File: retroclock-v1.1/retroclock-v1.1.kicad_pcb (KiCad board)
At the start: 4 copper layers, 147.5 x 108 mm, 22 parts, among them J1 Hours, J2 Mins, J3 Secs, J4 Nixie YY2, J5 Nixie YY1, J6 Nixie MM2, J7 Nixie MM1, J8 Nixie DD2, J9 Nixie DD1

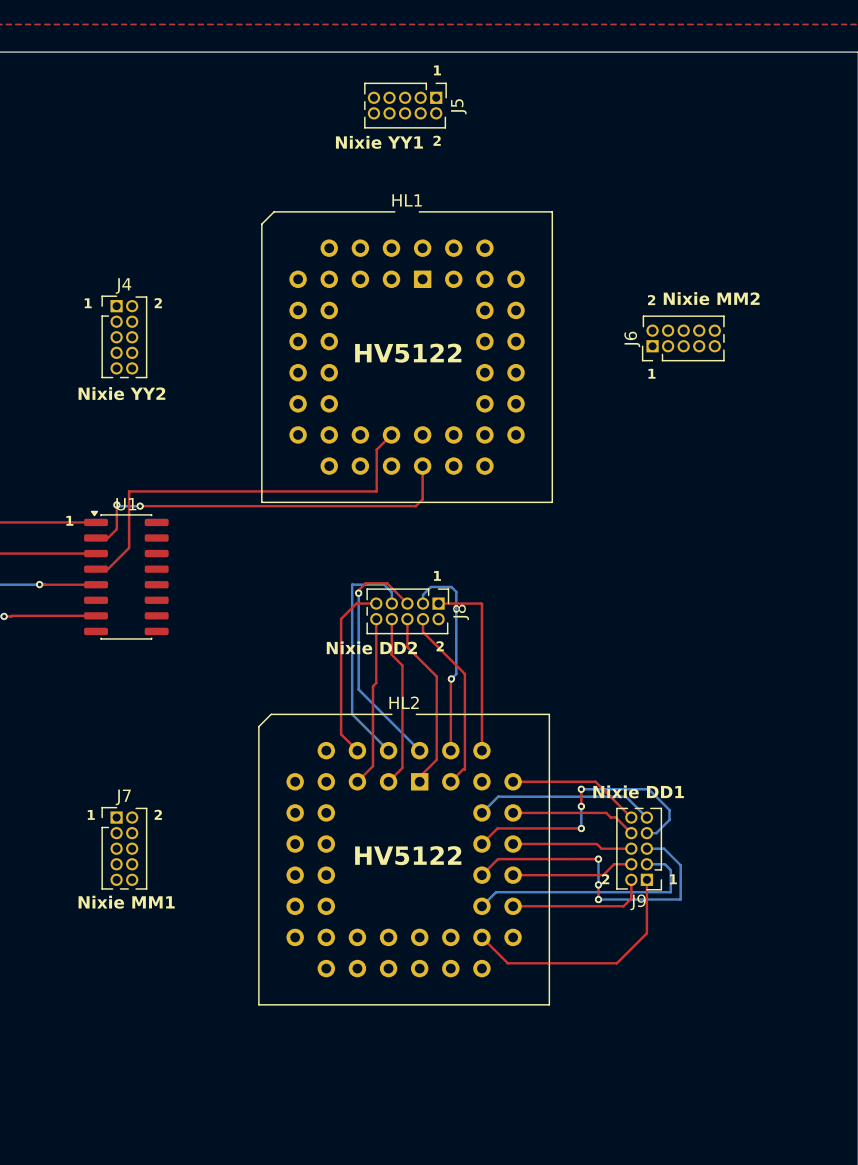
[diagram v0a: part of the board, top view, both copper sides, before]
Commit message: finished routing, no errors
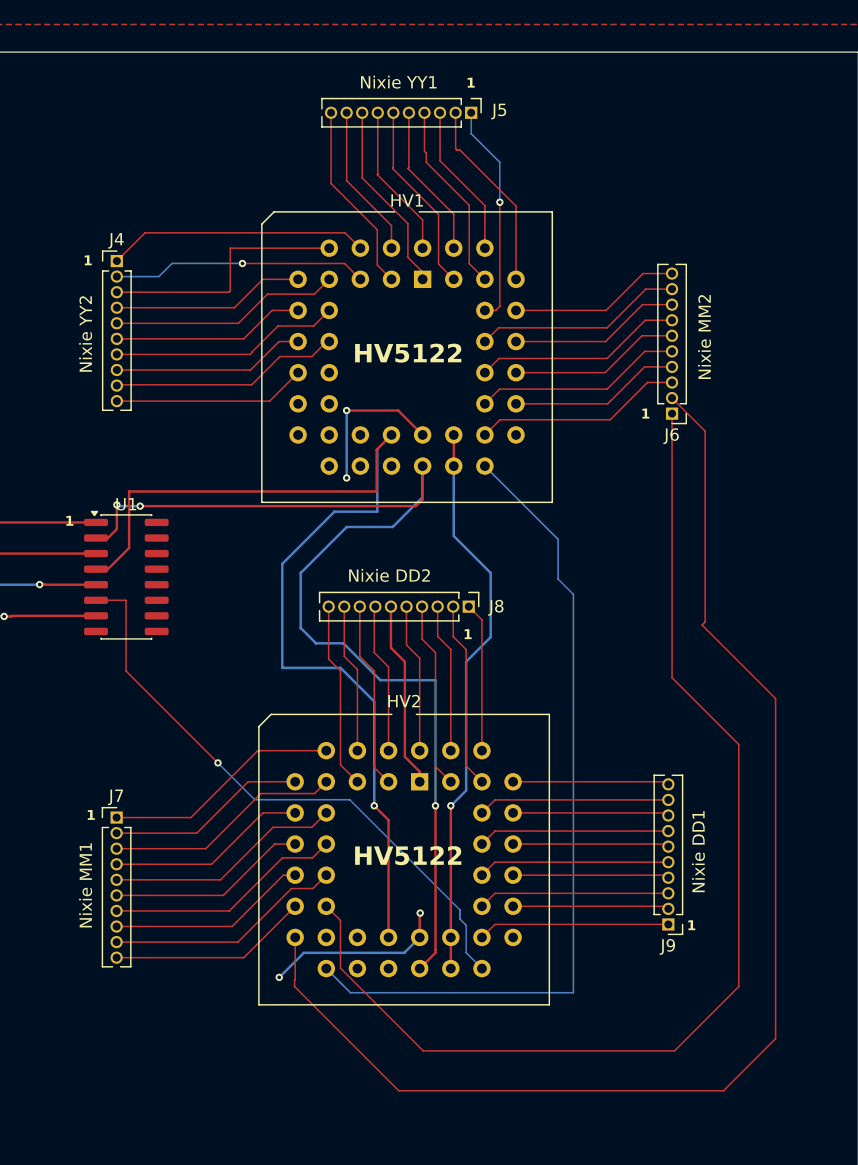
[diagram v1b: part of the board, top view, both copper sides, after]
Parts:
- J4, J5, J6, J7, J8, J9: footprint Connector_PinHeader_1.27mm:PinHeader_2x05_P1.27mm_Vertical -> Connector_PinHeader_1.27mm:PinHeader_1x10_P1.27mm_Vertical
- moved J6 5.73 mm to (208.8, 67.8), turned to 180 degrees
- moved J9 4.04 mm to (208.5, 109.4)
- moved J4 3.68 mm to (163.5, 55.3)
- moved J5 3.10 mm to (192.4, 43.2)
- moved J8 2.48 mm to (192.2, 83.5)
- renumbered HL1 to HV1, HL2 to HV2
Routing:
- net Net-(J6-Pin_2): track 0.00 -> 104.5 mm
- net Net-(HL2-HVO31): track 0.00 -> 92.0 mm
- net Net-(HL1-D_IN): track 0.00 -> 66.9 mm
- net Net-(HL1-CLK): track 31.9 -> 88.3 mm, vias 2 -> 3
- net Net-(HL1-OE): track 33.3 -> 86.5 mm, vias 0 -> 1
- net Net-(HL2-D_IN): track 0.00 -> 49.1 mm, vias 0 -> 1
- net +12V: track 0.00 -> 46.1 mm, vias 0 -> 1
- net GND: track 0.00 -> 27.4 mm, vias 0 -> 4
- net Net-(HL1-HVO19): track 0.00 -> 21.3 mm
- net Net-(HL1-HVO21): track 0.00 -> 20.9 mm
- net Net-(HL1-HVO20): track 0.00 -> 20.8 mm, vias 0 -> 1
- net Net-(HL2-HVO29): track 0.00 -> 19.4 mm
- net Net-(HL2-HVO25): track 0.00 -> 19.4 mm
- net Net-(J7-Pin_3): track 0.00 -> 19.4 mm
- net Net-(HL2-HVO27): track 0.00 -> 19.4 mm
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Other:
- board text added: "J8"
- board text removed: "2"

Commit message: retroclock 1.1 sent to JLCPCB!
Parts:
- added C10: 100nF, Capacitor_THT:C_Disc_D3.4mm_W2.1mm_P2.50mm, F.Cu at (144.3, 84.0)
- added C11: 100nF, Capacitor_THT:C_Disc_D3.4mm_W2.1mm_P2.50mm, F.Cu at (161.8, 107.3)
- added C12: 68uF, Capacitor_THT:CP_Radial_D8.0mm_P3.80mm, F.Cu at (161.4, 97.5)
- added C13: 100uF, Capacitor_THT:CP_Radial_D10.0mm_P5.00mm, F.Cu at (126.5, 97.3)
- added C14: 100nF, Capacitor_THT:C_Rect_L18.0mm_W7.0mm_P15.00mm_FKS3_FKP3, F.Cu at (118.8, 98.8)
- added C15: 10uF, Capacitor_THT:CP_Radial_D8.0mm_P3.80mm, F.Cu at (132.0, 78.0)
- added C16: 10uF, Capacitor_THT:CP_Radial_D8.0mm_P3.80mm, F.Cu at (146.0, 72.4)
- added C4: 100n, Capacitor_THT:C_Disc_D3.4mm_W2.1mm_P2.50mm, F.Cu at (173.3, 89.2)
- added C5: 100n, Capacitor_SMD:C_1206_3216Metric_Pad1.33x1.80mm_HandSolder, B.Cu at (205.2, 90.0)
- added C6: 100n, Capacitor_THT:C_Disc_D3.4mm_W2.1mm_P2.50mm, F.Cu at (178.6, 91.8)
- added C7: 100n, Capacitor_SMD:C_1206_3216Metric_Pad1.33x1.80mm_HandSolder, B.Cu at (208.7, 68.5)
- added C8: 100n, Capacitor_THT:C_Disc_D3.4mm_W2.1mm_P2.50mm, F.Cu at (183.4, 111.4)
- added C9: 100n, Capacitor_THT:C_Disc_D3.4mm_W2.1mm_P2.50mm, F.Cu at (177.6, 111.4)
- added D1: LED, LED_THT:LED_D3.0mm_Clear, F.Cu at (191.2, 46.5)
- added D2: LED, LED_THT:LED_D3.0mm_Clear, F.Cu at (128.9, 67.8)
- added D3: RF01VM2S, Diode_THT:D_DO-15_P15.24mm_Horizontal, F.Cu at (125.8, 110.3)
- added D4: LED, LED_THT:LED_D3.0mm_Clear, F.Cu at (172.2, 111.4)
- added D5: LED, LED_THT:LED_D3.0mm_Clear, F.Cu at (187.1, 111.4)
- added DCFRx1: ~, 01_mjc_library:DCF77Rx_A, F.Cu at (121.6, 50.0)
- added G***: LOGO, 01_mjc_library:doomsday_clock, F.Cu at (139.5, 48.3)
- added H1: MountingHole, MountingHole:MountingHole_2.2mm_M2_Pad, F.Cu at (81.0, 45.0)
- added H2: MountingHole, MountingHole:MountingHole_2.2mm_M2_Pad, F.Cu at (81.0, 114.0)
- added H3: MountingHole, MountingHole:MountingHole_2.2mm_M2_Pad, F.Cu at (227.0, 45.0)
- added H4: MountingHole, MountingHole:MountingHole_2.2mm_M2_Pad, F.Cu at (227.0, 114.0)
- added J10: Serial DBG, Connector_PinHeader_2.54mm:PinHeader_1x03_P2.54mm_Vertical, F.Cu at (181.0, 50.6)
- added J11: DCF DBG, Connector_Molex:Molex_KK-254_AE-6410-02A_1x02_P2.54mm_Vertical, F.Cu at (119.2, 65.8)
- added J12: Supply, Connector_Molex:Molex_KK-254_AE-6410-03A_1x03_P2.54mm_Vertical, F.Cu at (174.5, 104.2)
- added J13: 170V, Connector_Molex:Molex_KK-254_AE-6410-02A_1x02_P2.54mm_Vertical, F.Cu at (117.3, 105.0)
- added J14: ~, 01_mjc_library:Jumper 2.54 2x03, F.Cu at (160.0, 86.4)
- added J15: 3v3 src, Connector_PinHeader_2.54mm:PinHeader_1x03_P2.54mm_Vertical, F.Cu at (151.9, 77.0)
- added L1: 100H, Inductor_THT:L_Radial_D10.0mm_P5.00mm_Neosid_SD12k_style3, F.Cu at (153.8, 107.5)
- added LVL1: ~, Package_SO:SOIC-16_3.9x9.9mm_P1.27mm, F.Cu at (175.9, 81.7)
- added MAX1: MAX1771, Package_SO:SOIC-8_3.9x4.9mm_P1.27mm, F.Cu at (148.3, 89.0)
- added Q1: ~, 01_mjc_library:MOSFET, F.Cu at (148.1, 97.3)
- added R10: 1.2M, Resistor_THT:R_Axial_DIN0204_L3.6mm_D1.6mm_P7.62mm_Horizontal, F.Cu at (126.0, 105.0)
- added R11: 10k, Resistor_THT:R_Axial_DIN0204_L3.6mm_D1.6mm_P7.62mm_Horizontal, F.Cu at (137.8, 105.0)
- added R12: 0.2, Resistor_THT:R_Axial_DIN0204_L3.6mm_D1.6mm_P7.62mm_Horizontal, F.Cu at (137.4, 84.5)
- added R13: R, Resistor_THT:R_Axial_DIN0204_L3.6mm_D1.6mm_P7.62mm_Horizontal, F.Cu at (98.7, 46.9)
- added R14: R, Resistor_THT:R_Axial_DIN0204_L3.6mm_D1.6mm_P7.62mm_Horizontal, F.Cu at (98.7, 52.9)
- added R15: R, Resistor_THT:R_Axial_DIN0204_L3.6mm_D1.6mm_P7.62mm_Horizontal, F.Cu at (98.7, 68.3)
- added R16: R, Resistor_THT:R_Axial_DIN0204_L3.6mm_D1.6mm_P7.62mm_Horizontal, F.Cu at (98.8, 74.3)
- added R17: R, Resistor_THT:R_Axial_DIN0204_L3.6mm_D1.6mm_P7.62mm_Horizontal, F.Cu at (94.9, 97.5)
- added R18: R, Resistor_THT:R_Axial_DIN0204_L3.6mm_D1.6mm_P7.62mm_Horizontal, F.Cu at (101.4, 97.5)
- added R19: R, Resistor_THT:R_Axial_DIN0204_L3.6mm_D1.6mm_P7.62mm_Horizontal, F.Cu at (170.1, 115.9)
- added R20: R, Resistor_THT:R_Axial_DIN0204_L3.6mm_D1.6mm_P7.62mm_Horizontal, F.Cu at (188.4, 115.9)
- added R7: R, Resistor_THT:R_Axial_DIN0204_L3.6mm_D1.6mm_P7.62mm_Horizontal, F.Cu at (185.6, 52.0)
- added R8: R, Resistor_THT:R_Axial_DIN0204_L3.6mm_D1.6mm_P7.62mm_Horizontal, F.Cu at (123.9, 69.4)
- added R9: 0.2, Resistor_THT:R_Axial_DIN0204_L3.6mm_D1.6mm_P7.62mm_Horizontal, F.Cu at (137.3, 88.8)
- C1, C2, C3: footprint Capacitor_THT:CP_Axial_L18.0mm_D6.5mm_P25.00mm_Horizontal -> Capacitor_THT:C_Axial_L19.0mm_D7.5mm_P25.00mm_Horizontal
- ESP1: footprint mjc_library:ESP32 Header -> 01_mjc_library:ESP32 Header
- HV1, HV2: footprint mjc_library:PLCC-44_THT-Socket -> 01_mjc_library:PLCC44 MillMaxMfg 940
- J1, J2, J3: footprint Connector_PinHeader_1.27mm:PinHeader_1x02_P1.27mm_Vertical -> Connector_Molex:Molex_KK-254_AE-6410-02A_1x02_P2.54mm_Vertical
- J4, J6, J7, J8: footprint Connector_PinHeader_1.27mm:PinHeader_1x10_P1.27mm_Vertical -> Connector_PinHeader_2.54mm:PinHeader_2x07_P2.54mm_Vertical
- J5: value Nixie YY1 -> Nixie DD1; footprint Connector_PinHeader_1.27mm:PinHeader_1x10_P1.27mm_Vertical -> Connector_PinHeader_2.54mm:PinHeader_2x07_P2.54mm_Vertical
- J9: value Nixie DD1 -> Nixie YY1; footprint Connector_PinHeader_1.27mm:PinHeader_1x10_P1.27mm_Vertical -> Connector_PinHeader_2.54mm:PinHeader_2x07_P2.54mm_Vertical
- R1, R2, R3, R4, R5, R6: footprint Resistor_THT:R_Axial_DIN0207_L6.3mm_D2.5mm_P7.62mm_Horizontal -> Resistor_THT:R_Axial_DIN0204_L3.6mm_D1.6mm_P7.62mm_Horizontal
- U1: footprint Package_SO:SOIC-16_3.9x9.9mm_P1.27mm -> 01_mjc_library:HT7333
- moved J4 79.2 mm to (228.3, 100.9), turned to 180 degrees
- moved J7 46.5 mm to (184.9, 59.4)
- moved HV1 46.0 mm to (205.8, 99.4), turned to 180 degrees
- moved J5 46.0 mm to (228.3, 71.9), turned to 180 degrees
- moved J8 44.4 mm to (214.3, 45.0)
- moved HV2 43.4 mm to (208.3, 59.3)
- moved J6 31.7 mm to (185.0, 88.7), turned to 0 degrees
- moved ESP1 27.3 mm to (162.9, 59.8)
- moved U1 25.2 mm to (139.3, 78.3)
- moved C1 18.0 mm to (106.2, 61.9), turned to 180 degrees
- moved C2 17.2 mm to (106.4, 83.3), turned to 180 degrees
- moved C3 16.7 mm to (106.2, 106.4), turned to 180 degrees
- moved R3 12.5 mm to (98.7, 71.3)
- moved J3 11.9 mm to (83.4, 97.9), turned to 90 degrees
- moved J2 11.9 mm to (84.5, 74.0), turned to 90 degrees
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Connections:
- net Net-(ESP1-G10) renamed AM_HRS
- net Net-(ESP1-G20) renamed AM_MIN
- net Net-(ESP1-G21) renamed AM_SEC
- net Net-(J1-Pin_2) renamed /ammeter_driver/AM_H-
- net Net-(J2-Pin_2) renamed /ammeter_driver/AM_M-
- net Net-(J3-Pin_2) renamed /ammeter_driver/AM_S-
- ESP1 pad 1: Net-(ESP1-G5) -> /OE
- ESP1 pad 10: unconnected-(ESP1-G1/A1_1-Pad10) -> /BOOST_EN
- ESP1 pad 3: unconnected-(ESP1-G7-Pad3) -> DCF_PON
- ESP1 pad 4: Net-(ESP1-SDA) -> /SDA
- ESP1 pad 5: Net-(ESP1-SCL) -> /SCL
- ESP1 pad 9: unconnected-(ESP1-G0/A1_0-Pad9) -> DCF_DAT
- HV1 pad 1: Net-(HL1-HVO16) -> Net-(HV1-HVO16)
- HV1 pad 10: Net-(HL1-HVO25) -> Net-(HV1-HVO25)
- HV1 pad 11: Net-(HL1-HVO26) -> Net-(HV1-HVO26)
- HV1 pad 12: Net-(HL1-HVO27) -> Net-(HV1-HVO27)
- HV1 pad 13: Net-(HL1-HVO28) -> Net-(HV1-HVO28)
- HV1 pad 14: unconnected-(HL1-HVO29-Pad14) -> Net-(HV1-HVO29)
- HV1 pad 15: unconnected-(HL1-HVO30-Pad15) -> Net-(HV1-HVO30)
- HV1 pad 16: unconnected-(HL1-HVO31-Pad16) -> Net-(HV1-HVO31)
- HV1 pad 2: Net-(HL1-HVO17) -> Net-(HV1-HVO17)
- HV1 pad 23: Net-(HL1-OE) -> NIX_OE
- HV1 pad 24: Net-(HL1-CLK) -> NIX_CLK
- HV1 pad 3: Net-(HL1-HVO18) -> Net-(HV1-HVO18)
- HV1 pad 30: Net-(HL1-HVO1) -> Net-(HV1-HVO1)
- HV1 pad 31: Net-(HL1-HVO2) -> Net-(HV1-HVO2)
- HV1 pad 32: Net-(HL1-HVO3) -> Net-(HV1-HVO3)
- HV1 pad 33: Net-(HL1-HVO4) -> Net-(HV1-HVO4)
- HV1 pad 34: Net-(HL1-HVO5) -> Net-(HV1-HVO5)
- HV1 pad 35: Net-(HL1-HVO6) -> Net-(HV1-HVO6)
- HV1 pad 36: Net-(HL1-HVO7) -> Net-(HV1-HVO7)
- HV1 pad 37: Net-(HL1-HVO8) -> Net-(HV1-HVO8)
- HV1 pad 38: Net-(HL1-HVO9) -> Net-(HV1-HVO9)
- HV1 pad 39: Net-(HL1-HVO10) -> Net-(HV1-HVO10)
- HV1 pad 4: Net-(HL1-HVO19) -> Net-(HV1-HVO19)
- HV1 pad 40: Net-(HL1-HVO11) -> Net-(HV1-HVO11)
- HV1 pad 41: Net-(HL1-HVO12) -> Net-(HV1-HVO12)
- HV1 pad 42: Net-(HL1-HVO13) -> Net-(HV1-HVO13)
- HV1 pad 43: Net-(HL1-HVO14) -> Net-(HV1-HVO14)
- HV1 pad 44: Net-(HL1-HVO15) -> Net-(HV1-HVO15)
- HV1 pad 5: Net-(HL1-HVO20) -> Net-(HV1-HVO20)
- HV1 pad 6: Net-(HL1-HVO21) -> unconnected-(HV1-HVO21-Pad6)
- HV1 pad 7: Net-(HL1-HVO22) -> Net-(HV1-HVO22)
- HV1 pad 8: Net-(J4-Pin_5) -> Net-(HV1-HVO23)
- HV1 pad 9: Net-(HL1-HVO24) -> Net-(HV1-HVO24)
- HV2 pad 10: Net-(HL2-HVO25) -> Net-(HV2-HVO25)
- HV2 pad 11: Net-(HL2-HVO26) -> Net-(HV2-HVO26)
- HV2 pad 12: Net-(HL2-HVO27) -> Net-(HV2-HVO27)
- HV2 pad 13: Net-(HL2-HVO28) -> Net-(HV2-HVO28)
- HV2 pad 14: Net-(HL2-HVO29) -> Net-(HV2-HVO29)
- HV2 pad 15: Net-(HL2-HVO30) -> Net-(HV2-HVO30)
- HV2 pad 16: Net-(HL2-HVO31) -> Net-(HV2-HVO31)
- HV2 pad 17: Net-(J6-Pin_2) -> unconnected-(HV2-HVO32-Pad17)
- HV2 pad 23: Net-(HL1-OE) -> NIX_OE
- HV2 pad 24: Net-(HL1-CLK) -> NIX_CLK
- HV2 pad 28: Net-(HL2-D_IN) -> NIX_DAT_IN
- HV2 pad 30: Net-(HL2-HVO1) -> Net-(HV2-HVO1)
- HV2 pad 31: Net-(HL2-HVO2) -> Net-(HV2-HVO2)
- HV2 pad 32: Net-(HL2-HVO3) -> Net-(HV2-HVO3)
- HV2 pad 33: Net-(HL2-HVO4) -> Net-(HV2-HVO4)
- HV2 pad 34: Net-(HL2-HVO5) -> Net-(HV2-HVO5)
- HV2 pad 35: Net-(HL2-HVO6) -> Net-(HV2-HVO6)
- HV2 pad 36: Net-(HL2-HVO7) -> Net-(HV2-HVO7)
- HV2 pad 37: Net-(HL2-HVO8) -> Net-(HV2-HVO8)
- HV2 pad 38: Net-(HL2-HVO9) -> Net-(HV2-HVO9)
- HV2 pad 39: Net-(HL2-HVO10) -> Net-(HV2-HVO10)
- HV2 pad 6: Net-(HL2-HVO21) -> unconnected-(HV2-HVO21-Pad6)
- HV2 pad 7: Net-(HL2-HVO22) -> Net-(HV2-HVO22)
- HV2 pad 8: Net-(J7-Pin_3) -> Net-(HV2-HVO23)
- HV2 pad 9: Net-(HL2-HVO24) -> Net-(HV2-HVO24)
- J4 pad 1: Net-(HL1-HVO19) -> Net-(HV1-HVO22)
- J4 pad 10: Net-(HL1-HVO28) -> Net-(HV1-HVO31)
- J4 pad 2: Net-(HL1-HVO20) -> Net-(HV1-HVO23)
- J4 pad 3: Net-(HL1-HVO21) -> Net-(HV1-HVO24)
- J4 pad 4: Net-(HL1-HVO22) -> Net-(HV1-HVO25)
- J4 pad 5: Net-(J4-Pin_5) -> Net-(HV1-HVO26)
- J4 pad 6: Net-(HL1-HVO24) -> Net-(HV1-HVO27)
- J4 pad 7: Net-(HL1-HVO25) -> Net-(HV1-HVO28)
- J4 pad 8: Net-(HL1-HVO26) -> Net-(HV1-HVO29)
- J4 pad 9: Net-(HL1-HVO27) -> Net-(HV1-HVO30)
- J5 pad 1: Net-(HL1-HVO9) -> Net-(HV2-HVO1)
- J5 pad 10: Net-(HL1-HVO18) -> Net-(HV2-HVO10)
- J5 pad 2: Net-(HL1-HVO10) -> Net-(HV2-HVO2)
- J5 pad 3: Net-(HL1-HVO11) -> Net-(HV2-HVO3)
- J5 pad 4: Net-(HL1-HVO12) -> Net-(HV2-HVO4)
- J5 pad 5: Net-(HL1-HVO13) -> Net-(HV2-HVO5)
- J5 pad 6: Net-(HL1-HVO14) -> Net-(HV2-HVO6)
- J5 pad 7: Net-(HL1-HVO15) -> Net-(HV2-HVO7)
- J5 pad 8: Net-(HL1-HVO16) -> Net-(HV2-HVO8)
- J5 pad 9: Net-(HL1-HVO17) -> Net-(HV2-HVO9)
- J6 pad 1: Net-(HL2-HVO31) -> Net-(HV1-HVO1)
- J6 pad 10: Net-(HL1-HVO8) -> Net-(HV1-HVO10)
- J6 pad 2: Net-(J6-Pin_2) -> Net-(HV1-HVO2)
- J6 pad 3: Net-(HL1-HVO1) -> Net-(HV1-HVO3)
- J6 pad 4: Net-(HL1-HVO2) -> Net-(HV1-HVO4)
- J6 pad 5: Net-(HL1-HVO3) -> Net-(HV1-HVO5)
- J6 pad 6: Net-(HL1-HVO4) -> Net-(HV1-HVO6)
- J6 pad 7: Net-(HL1-HVO5) -> Net-(HV1-HVO7)
- J6 pad 8: Net-(HL1-HVO6) -> Net-(HV1-HVO8)
- J6 pad 9: Net-(HL1-HVO7) -> Net-(HV1-HVO9)
- J7 pad 1: Net-(HL2-HVO21) -> Net-(HV2-HVO22)
- J7 pad 10: Net-(HL2-HVO30) -> Net-(HV2-HVO31)
- J7 pad 2: Net-(HL2-HVO22) -> Net-(HV2-HVO23)
- J7 pad 3: Net-(J7-Pin_3) -> Net-(HV2-HVO24)
- J7 pad 4: Net-(HL2-HVO24) -> Net-(HV2-HVO25)
- J7 pad 5: Net-(HL2-HVO25) -> Net-(HV2-HVO26)
- J7 pad 6: Net-(HL2-HVO26) -> Net-(HV2-HVO27)
- J7 pad 7: Net-(HL2-HVO27) -> Net-(HV2-HVO28)
- J7 pad 8: Net-(HL2-HVO28) -> Net-(HV2-HVO29)
- J7 pad 9: Net-(HL2-HVO29) -> Net-(HV2-HVO30)
- J9 pad 1: Net-(HL2-HVO1) -> Net-(HV1-HVO11)
- J9 pad 10: Net-(HL2-HVO10) -> Net-(HV1-HVO20)
- J9 pad 2: Net-(HL2-HVO2) -> Net-(HV1-HVO12)
- J9 pad 3: Net-(HL2-HVO3) -> Net-(HV1-HVO13)
- J9 pad 4: Net-(HL2-HVO4) -> Net-(HV1-HVO14)
- J9 pad 5: Net-(HL2-HVO5) -> Net-(HV1-HVO15)
- J9 pad 6: Net-(HL2-HVO6) -> Net-(HV1-HVO16)
- J9 pad 7: Net-(HL2-HVO7) -> Net-(HV1-HVO17)
- J9 pad 8: Net-(HL2-HVO8) -> Net-(HV1-HVO18)
- J9 pad 9: Net-(HL2-HVO9) -> Net-(HV1-HVO19)
- U1 pad 1: +3V3 -> GND
- U1 pad 2: Net-(HL1-CLK) -> +12V
- U1 pad 3: Net-(ESP1-SCL) -> Net-(J15-Pin_1)
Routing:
- net +12V: track 46.1 -> 209.9 mm, vias 1 -> 0
- net Net-(J6-Pin_2): track 104.5 -> 0.00 mm
- net DCF_DAT: track 0.00 -> 98.6 mm
- net Net-(HL2-HVO31): track 92.0 -> 0.00 mm
- net Net-(HL1-CLK): track 88.3 -> 0.00 mm, vias 3 -> 0
- net Net-(HL1-OE): track 86.5 -> 0.00 mm, vias 1 -> 0
- net /SCL: track 0.00 -> 84.1 mm, vias 0 -> 3
- net /SDA: track 0.00 -> 74.9 mm, vias 0 -> 1
- net Net-(ESP1-G5): track 63.2 -> 0.00 mm, vias 1 -> 0
- net Net-(ESP1-SDA): track 59.9 -> 0.00 mm, vias 1 -> 0
- net Net-(J12-Pin_2): track 0.00 -> 58.5 mm
- net +3V3: track 131.7 -> 189.9 mm
- net Net-(HV1-D_IN): track 66.9 -> 9.66 mm
- net /OE: track 0.00 -> 55.4 mm, vias 0 -> 1
- net Net-(ESP1-SCL): track 51.0 -> 0.00 mm, vias 1 -> 0
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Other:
- board size 147.5 x 108 mm -> 156.7 x 79.2 mm
- copper layers 4 -> 2
- board text added: "+"
- board text added: "-"
- board text added: "12V"
- board text added: "12V to 170V Boost"
- board text added: "170V"
- board text added: "2026-03-06"
- board text added: "3V3"
- board text added: "DAT"
- board text added: "DCF DBG"
- board text added: "ESP"
- board text added: "ESP32 Super Mini"
- board text added: "EXT"
- board text added: "GND"
- board text added: "Hours"
- board text added: "INT"
- board text added: "JLCJLCJLC"
- board text added: "Mins"
- board text added: "OFF"
- board text added: "ON"
- board text added: "SCL"
- board text added: "SDA"
- board text added: "Secs"
- board text added: "jCAPS Corp"
- board text added: "retro clock (v1.1)"
- board text removed: "1"
